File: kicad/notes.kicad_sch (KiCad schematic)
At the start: 0 parts

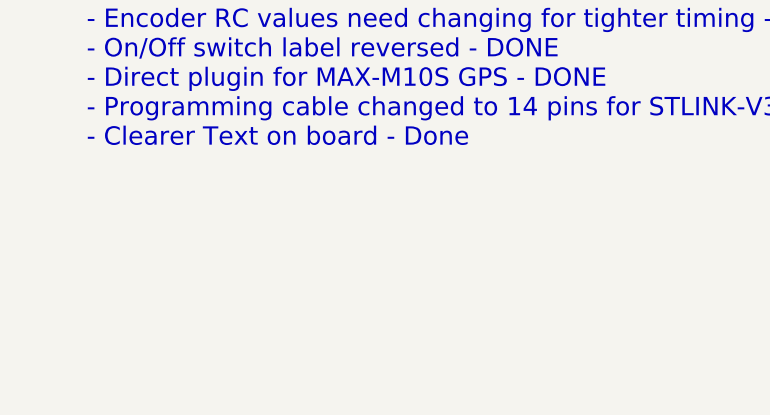
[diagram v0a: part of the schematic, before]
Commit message: Working on CM4 IO
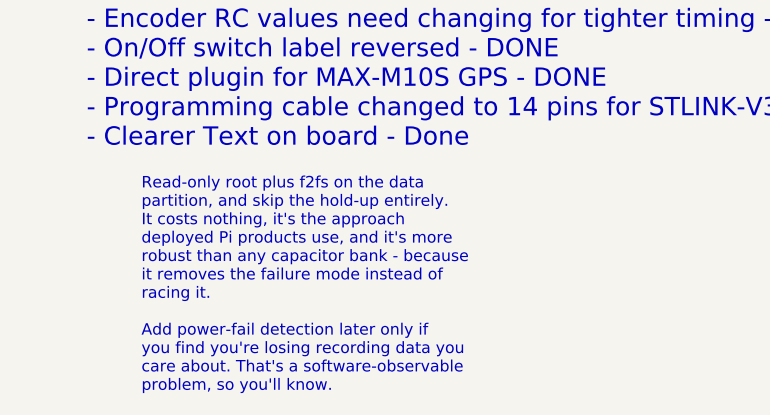
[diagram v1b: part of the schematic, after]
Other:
- note added: "Read-only root plus f2fs on the data partition, and skip the hold-up entirely. It costs nothing, it's the approach deployed Pi products use, and it's more robust than any capacitor bank - because it removes the failure mode instead of racing it. Add power-fail detection later only if you find you're losing recording data you care about. That's a software-observable problem, so you'll know."
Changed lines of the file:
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@@
+		)
+	)
+	(text "Read-only root plus f2fs on the data \npartition, and skip the hold-up entirely. \nIt costs nothing, it's the approach \ndeployed Pi products use, and it's more \nrobust than any capacitor bank - because \nit removes the failure mode instead of \nracing it.\n\nAdd power-fail detection later only if \nyou find you're losing recording data you \ncare about. That's a software-observable \nproblem, so you'll know."
+		(exclude_from_sim no)
+		(at 34.29 181.356 0)
+		(effects
+			(font
+				(size 1.27 1.27)
+			)
+			(justify left)
 		)
 	)

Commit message: CM4 schematic changes, before renumbering
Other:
- note added: "CM4 power-fail strategy: read-only root plus f2fs on the data partition, and no hold-up capacitor bank. It costs nothing, it is the approach deployed Pi products use, and it removes the failure mode instead of racing it. Add power-fail detection later only if recording data is actually being lost. That is a software-observable problem, so it will be obvious."
- note added: "Changes for V2.0 - Add Raspberry Pi CM4 carrier (2x DF40C-100DS-0.4V) - Gigabit Ethernet, 2x USB 2.0 via USB2514B hub - micro-USB OTG for rpiboot eMMC programming - Remove RS485 device port, USART1 now goes to the CM4 - ADDR0-2 / CONFIG_SW repurposed as SW1-SW4 - 12V to 5V buck (AP64501) for CM4 and both USB ports"
- note added: "MCU Specifications Part Number: STM32G474RET6 Package: LQFP64 Clock: 170 MHz (16 MHz HSE, PLL /4 x85 /2) Flash: 512 KB RAM: 128 KB Speed and position commands are received from the on-board CM4 over USART1 (3.3V, full duplex). Modbus node address is fixed at 1 - the link is point-to-point, so there is no bus to address. Encoder is the E6B2-CWZ6C. Motor Controller: DM556Y. Program/debug: ST STDC14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"
- note added: "Purpose: Control dual axes of a motor controlled system, hosted by an on-board Raspberry Pi CM4. - Modbus RTU commands from the on-board CM4 over a 3.3V full-duplex UART (STM32 USART1) - MCU outputs motor PWM, direction, enable/disable - Input from encoder connected to motor output - Host provides configuration and position commands - MCU runs a PID loop to position/move motors - Onboard temperat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"
- note added: "This STM32 can be clocked up to 170MHz and runs at that speed. Reducing the clock was considered to weaken harmonics above 1GHz, but has not been implemented - every firmware revision to date runs at 170MHz. If RFI is ever measured as a real problem, the rate can be lowered in SystemClock_Config."
- note removed: "Changes for V1.1 - Encoder RC values need changing for tighter timing - DONE - On/Off switch label reversed - DONE - Direct plugin for MAX-M10S GPS - DONE - Programming cable changed to 14 pins for STLINK-V3MINIE -DONE - Clearer Text on board - Done"
- note removed: "MCU is the STM32G474CET6, 64-pin LQFP64 package Speed and position connands are received from a host over RS485. Encoder is the E6B2-CWZ6C. Motor Controller: DM556Y. 2-Wire program/debug connector with SWO. I2C for reading I2C sensors. 2 Limit switches. USART communication to Host. 16MHz oscillator, prescalers configures for 48MHz. MCU Specifications Part Number: STM32G474CET6 Package: LQFP64 Clo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"
- note removed: "Purpose: Control dual axes of a motor controlled system. - Modbus commands over isolated RS485 from a host. - MCU outputs motor PWM, direction, enable/disable - Input from encoder connected to motor output - Host provides configuration and position commands - MCU runs a PID loop to position/move motors - Onboard temperature sensor, MCU can turn fan on/off - I2C extender for sensors placed at the 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"
- note removed: "Read-only root plus f2fs on the data partition, and skip the hold-up entirely. It costs nothing, it's the approach deployed Pi products use, and it's more robust than any capacitor bank - because it removes the failure mode instead of racing it. Add power-fail detection later only if you find you're losing recording data you care about. That's a software-observable problem, so you'll know."
- note removed: "This STM32 can be clocked up to 170MHz. It was decided to decrease this to 48MHz due to RFI concerns. The 48MHz produces much weaker harmonics above 1GHz compared to 170MHz. If speed ever becomes a concern the clock rate can be increased."

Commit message: More mods
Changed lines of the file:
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@@
 	(text "CM4 power-fail strategy: read-only root\nplus f2fs on the data partition, and no\nhold-up capacitor bank. It costs nothing,\nit is the approach deployed Pi products\nuse, and it removes the failure mode\ninstead of racing it.\n\nAdd power-fail detection later only if\nrecording data is actually being lost.\nThat is a software-observable problem,\nso it will be obvious."
 		(exclude_from_sim no)
-		(at 34.29 181.356 0)
+		(at 33.782 173.482 0)
 		(effects
 			(font
@@
 	(text "Changes for V2.0\n\n- Add Raspberry Pi CM4 carrier (2x DF40C-100DS-0.4V)\n- Gigabit Ethernet, 2x USB 2.0 via USB2514B hub\n- micro-USB OTG for rpiboot eMMC programming\n- Remove RS485 device port, USART1 now goes to the CM4\n- ADDR0-2 / CONFIG_SW repurposed as SW1-SW4\n- 12V to 5V buck (AP64501) for CM4 and both USB ports"
 		(exclude_from_sim no)
-		(at 28.194 155.194 0)
+		(at 23.622 142.748 0)
 		(effects
 			(font
